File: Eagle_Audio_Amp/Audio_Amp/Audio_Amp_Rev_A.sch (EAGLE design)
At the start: 9 parts, among them IC1 LM386M-1

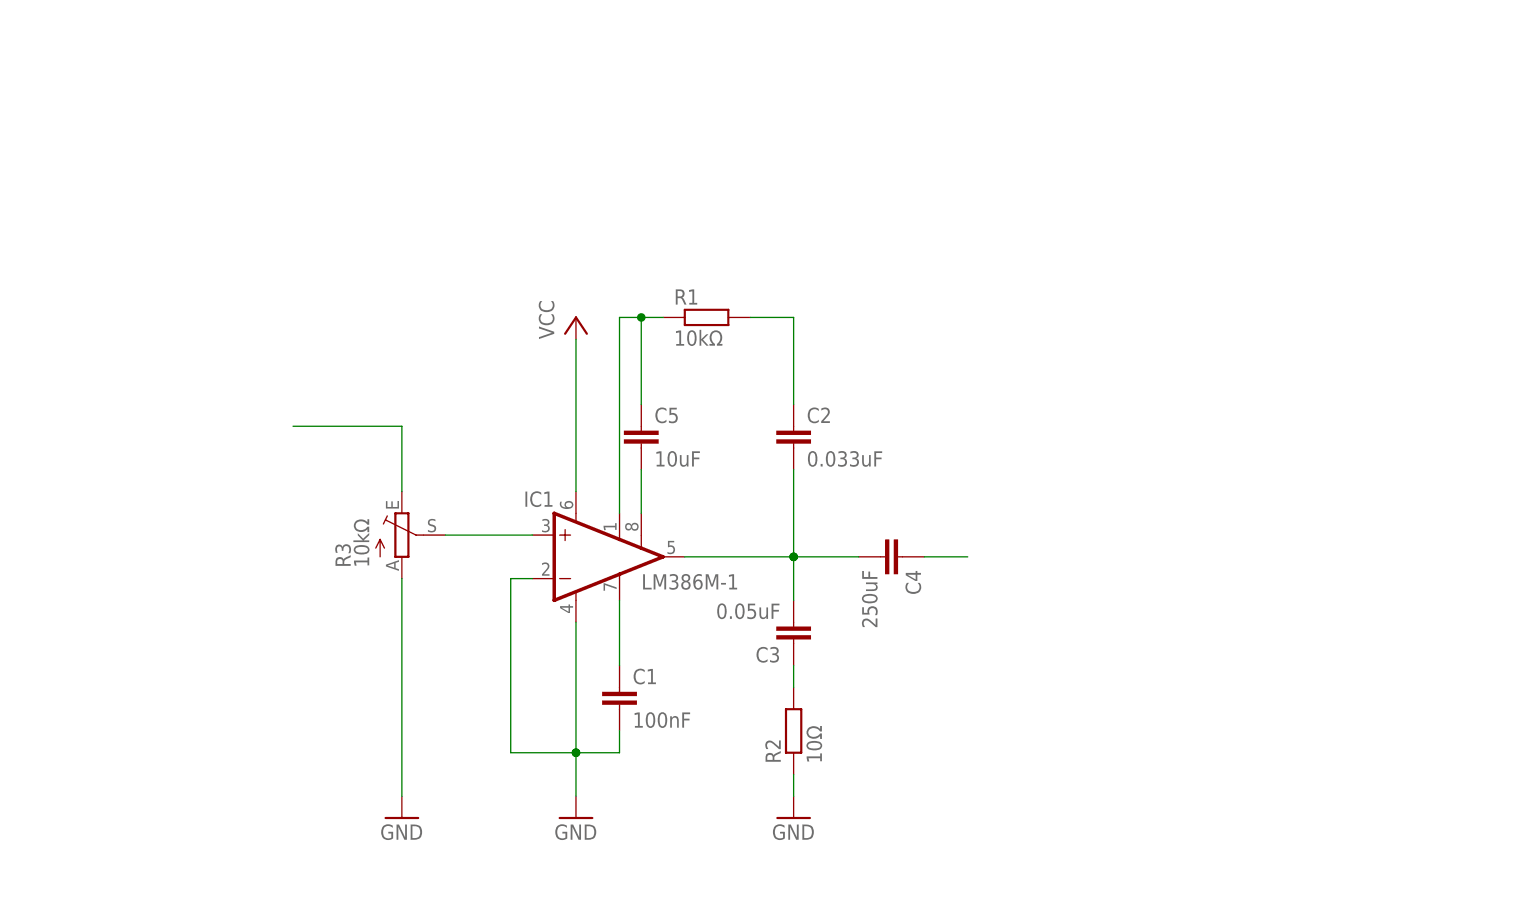
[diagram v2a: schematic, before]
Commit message: Add dummy speaker
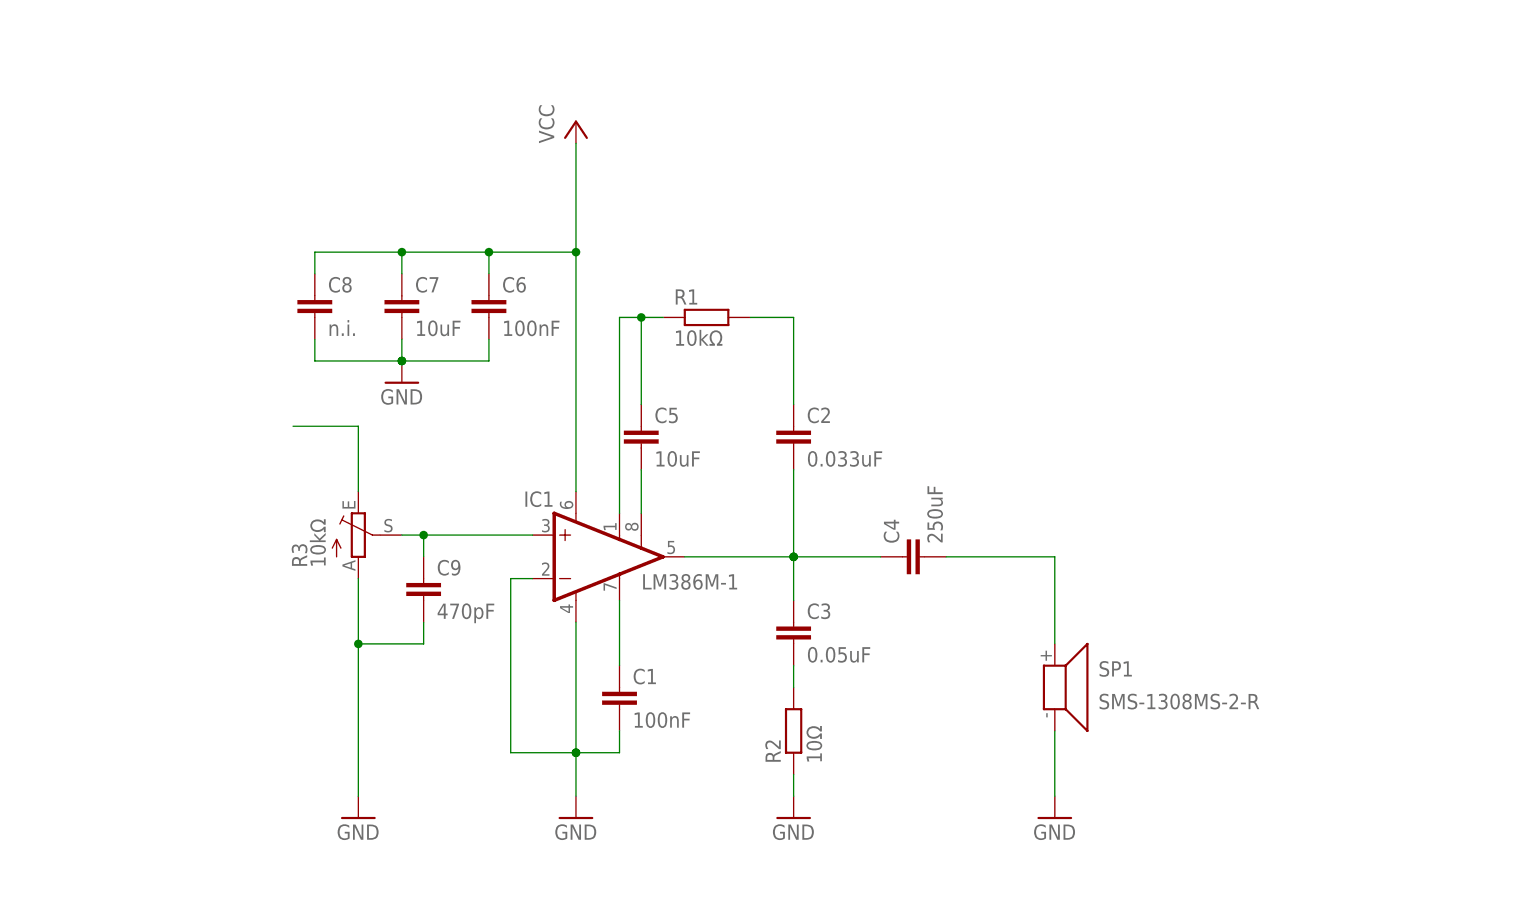
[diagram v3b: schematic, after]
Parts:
- added C6: 100nF, rcl:C-EUC0805
- added C7: 10uF, rcl:C-EUC0805
- added C8: n.i., rcl:C-EUC0805
- added C9: 470pF, rcl:C-EUC0805
- added SP1: SMS-1308MS-2-R, speaker:SMS-1308MS-2-R
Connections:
- net GND: now also C6.2, C7.2, C8.2, C9.2, SP1.2
- net N$2: now also C9.1
- net N$3: now also C3.1, C4.1; no longer C3.2, C4.2
- net N$6: now also C3.2; no longer C3.1
- net N$7: now also C4.2, SP1.1; no longer C4.1
- net VCC: now also C6.1, C7.1, C8.1
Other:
- moved on the sheet: C3, C4, R3
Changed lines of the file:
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@@
 <part name="GND4" library="supply1" deviceset="GND" device=""/>
 <part name="C5" library="rcl" deviceset="C-EU" device="C0805" value="10uF"/>
+<part name="C6" library="rcl" deviceset="C-EU" device="C0805" value="100nF"/>
+<part name="GND3" library="supply1" deviceset="GND" device=""/>
+<part name="C7" library="rcl" deviceset="C-EU" device="C0805" value="10uF"/>
+<part name="C8" library="rcl" deviceset="C-EU" device="C0805" value="n.i."/>
+<part name="C9" library="rcl" deviceset="C-EU" device="C0805" value="470pF"/>
+<part name="SP1" library="speaker" deviceset="SMS-1308MS-2-R" device=""/>
+<part name="GND5" library="supply1" deviceset="GND" device=""/>
 </parts>
 <sheets>
@@
 <instance part="C1" gate="G$1" x="93.98" y="40.64"/>
 <instance part="C2" gate="G$1" x="114.3" y="71.12"/>
-<instance part="C3" gate="G$1" x="114.3" y="45.72" rot="R180"/>
-<instance part="C4" gate="G$1" x="127" y="55.88" rot="R270"/>
-<instance part="GND1" gate="1" x="68.58" y="25.4"/>
+<instance part="C3" gate="G$1" x="114.3" y="48.26"/>
+<instance part="C4" gate="G$1" x="127" y="55.88" rot="R90"/>
+<instance part="GND1" gate="1" x="63.5" y="25.4"/>
 <instance part="GND2" gate="1" x="88.9" y="25.4"/>
-<instance part="P+1" gate="VCC" x="88.9" y="83.82"/>
-<instance part="R3" gate="1" x="68.58" y="58.42"/>
+<instance part="P+1" gate="VCC" x="88.9" y="106.68"/>
+<instance part="R3" gate="1" x="63.5" y="58.42"/>
 <instance part="R2" gate="G$1" x="114.3" y="35.56" rot="R90"/>
 <instance part="GND4" gate="1" x="114.3" y="25.4"/>
 <instance part="C5" gate="G$1" x="96.52" y="71.12"/>
+<instance part="C6" gate="G$1" x="78.74" y="86.36"/>
+<instance part="GND3" gate="1" x="68.58" y="76.2"/>
+<instance part="C7" gate="G$1" x="68.58" y="86.36"/>
+<instance part="C8" gate="G$1" x="58.42" y="86.36"/>
+<instance part="C9" gate="G$1" x="71.12" y="53.34"/>
+<instance part="SP1" gate="A" x="144.78" y="40.64"/>
+<instance part="GND5" gate="1" x="144.78" y="25.4"/>
 </instances>
 <busses>
@@
 <segment>
 <pinref part="IC1" gate="G$1" pin="+IN"/>
-<wire x1="83.82" y1="58.42" x2="73.66" y2="58.42" width="0.1524" layer="91"/>
+<wire x1="83.82" y1="58.42" x2="71.12" y2="58.42" width="0.1524" layer="91"/>
 <pinref part="R3" gate="1" pin="S"/>
+<pinref part="C9" gate="G$1" pin="1"/>
+<wire x1="71.12" y1="58.42" x2="68.58" y2="58.42" width="0.1524" layer="91"/>
+<wire x1="71.12" y1="55.88" x2="71.12" y2="58.42" width="0.1524" layer="91"/>
+<junction x="71.12" y="58.42"/>
 </segment>
 </net>
@@
 <pinref part="GND1" gate="1" pin="GND"/>
 <pinref part="R3" gate="1" pin="A"/>
-<wire x1="68.58" y1="27.94" x2="68.58" y2="53.34" width="0.1524" layer="91"/>
+<wire x1="63.5" y1="27.94" x2="63.5" y2="45.72" width="0.1524" layer="91"/>
+<pinref part="C9" gate="G$1" pin="2"/>
+<wire x1="63.5" y1="45.72" x2="63.5" y2="53.34" width="0.1524" layer="91"/>
+<wire x1="71.12" y1="48.26" x2="71.12" y2="45.72" width="0.1524" layer="91"/>
+<wire x1="71.12" y1="45.72" x2="63.5" y2="45.72" width="0.1524" layer="91"/>
+<junction x="63.5" y="45.72"/>
+</segment>
+<segment>
+<pinref part="C6" gate="G$1" pin="2"/>
+<pinref part="GND3" gate="1" pin="GND"/>
+<wire x1="78.74" y1="81.28" x2="78.74" y2="78.74" width="0.1524" layer="91"/>
+<wire x1="78.74" y1="78.74" x2="68.58" y2="78.74" width="0.1524" layer="91"/>
+<pinref part="C8" gate="G$1" pin="2"/>
+<wire x1="68.58" y1="78.74" x2="58.42" y2="78.74" width="0.1524" layer="91"/>
+<wire x1="58.42" y1="78.74" x2="58.42" y2="81.28" width="0.1524" layer="91"/>
+<junction x="68.58" y="78.74"/>
+<pinref part="C7" gate="G$1" pin="2"/>
+<wire x1="68.58" y1="78.74" x2="68.58" y2="81.28" width="0.1524" layer="91"/>
+<junction x="68.58" y="78.74"/>
+</segment>
+<segment>
+<pinref part="SP1" gate="A" pin="2"/>
+<wire x1="144.78" y1="35.56" x2="144.78" y2="27.94" width="0.1524" layer="91"/>
+<pinref part="GND5" gate="1" pin="GND"/>
 </segment>
 </net>
@@
 <pinref part="IC1" gate="G$1" pin="OUT"/>
 <wire x1="101.6" y1="55.88" x2="114.3" y2="55.88" width="0.1524" layer="91"/>
-<pinref part="C4" gate="G$1" pin="2"/>
 <junction x="114.3" y="55.88"/>
-<pinref part="C3" gate="G$1" pin="2"/>
-<wire x1="114.3" y1="55.88" x2="121.92" y2="55.88" width="0.1524" layer="91"/>
-<wire x1="114.3" y1="50.8" x2="114.3" y2="55.88" width="0.1524" layer="91"/>
 <junction x="114.3" y="55.88"/>
 <pinref part="C2" gate="G$1" pin="2"/>
 <wire x1="114.3" y1="55.88" x2="114.3" y2="66.04" width="0.1524" layer="91"/>
+<pinref part="C3" gate="G$1" pin="1"/>
+<wire x1="114.3" y1="55.88" x2="114.3" y2="50.8" width="0.1524" layer="91"/>
+<pinref part="C4" gate="G$1" pin="1"/>
+<wire x1="114.3" y1="55.88" x2="124.46" y2="55.88" width="0.1524" layer="91"/>
 </segment>
 </net>
@@
 </segment>
 </net>
-<net name="N$6" class="0">
-<segment>
-<pinref part="C3" gate="G$1" pin="1"/>
-<pinref part="R2" gate="G$1" pin="2"/>
-<wire x1="114.3" y1="43.18" x2="114.3" y2="40.64" width="0.1524" layer="91"/>
-</segment>
-</net>
 <net name="VCC" class="0">
 <segment>
 <pinref part="IC1" gate="G$1" pin="VS"/>
 <pinref part="P+1" gate="VCC" pin="VCC"/>
-<wire x1="88.9" y1="63.5" x2="88.9" y2="81.28" width="0.1524" layer="91"/>
-</segment>
-</net>
-<net name="N$7" class="0">
-<segment>
-<pinref part="C4" gate="G$1" pin="1"/>
-<wire x1="129.54" y1="55.88" x2="134.62" y2="55.88" width="0.1524" layer="91"/>
+<wire x1="88.9" y1="63.5" x2="88.9" y2="91.44" width="0.1524" layer="91"/>
+<pinref part="C6" gate="G$1" pin="1"/>
+<wire x1="88.9" y1="91.44" x2="88.9" y2="104.14" width="0.1524" layer="91"/>
+<wire x1="88.9" y1="91.44" x2="78.74" y2="91.44" width="0.1524" layer="91"/>
+<wire x1="78.74" y1="91.44" x2="78.74" y2="88.9" width="0.1524" layer="91"/>
+<junction x="88.9" y="91.44"/>
+<pinref part="C8" gate="G$1" pin="1"/>
+<wire x1="78.74" y1="91.44" x2="68.58" y2="91.44" width="0.1524" layer="91"/>
+<wire x1="68.58" y1="91.44" x2="58.42" y2="91.44" width="0.1524" layer="91"/>
+<wire x1="58.42" y1="91.44" x2="58.42" y2="88.9" width="0.1524" layer="91"/>
+<junction x="78.74" y="91.44"/>
+<pinref part="C7" gate="G$1" pin="1"/>
+<wire x1="68.58" y1="91.44" x2="68.58" y2="88.9" width="0.1524" layer="91"/>
+<junction x="68.58" y="91.44"/>
 </segment>
 </net>
@@
 <segment>
 <pinref part="R3" gate="1" pin="E"/>
-<wire x1="68.58" y1="63.5" x2="68.58" y2="71.12" width="0.1524" layer="91"/>
-<wire x1="68.58" y1="71.12" x2="55.88" y2="71.12" width="0.1524" layer="91"/>
+<wire x1="63.5" y1="63.5" x2="63.5" y2="71.12" width="0.1524" layer="91"/>
+<wire x1="63.5" y1="71.12" x2="55.88" y2="71.12" width="0.1524" layer="91"/>
 </segment>
 </net>
@@
 </segment>
 </net>
+<net name="N$6" class="0">
+<segment>
+<pinref part="C3" gate="G$1" pin="2"/>
+<pinref part="R2" gate="G$1" pin="2"/>
+<wire x1="114.3" y1="43.18" x2="114.3" y2="40.64" width="0.1524" layer="91"/>
+</segment>
+</net>
+<net name="N$7" class="0">
+<segment>
+<pinref part="C4" gate="G$1" pin="2"/>
+<wire x1="132.08" y1="55.88" x2="144.78" y2="55.88" width="0.1524" layer="91"/>
+<pinref part="SP1" gate="A" pin="1"/>
+<wire x1="144.78" y1="55.88" x2="144.78" y2="45.72" width="0.1524" layer="91"/>
+</segment>
+</net>
